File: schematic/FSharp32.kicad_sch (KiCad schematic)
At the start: 17 parts

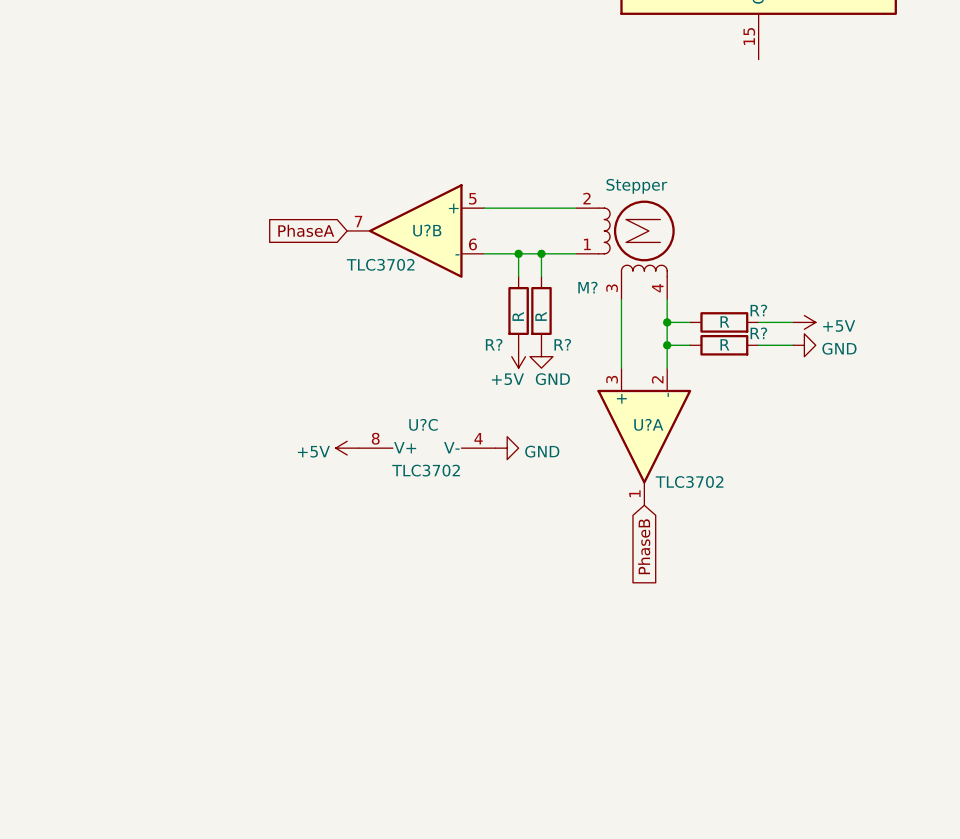
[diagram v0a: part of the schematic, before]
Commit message: continued schematic (finished rotary encoder)
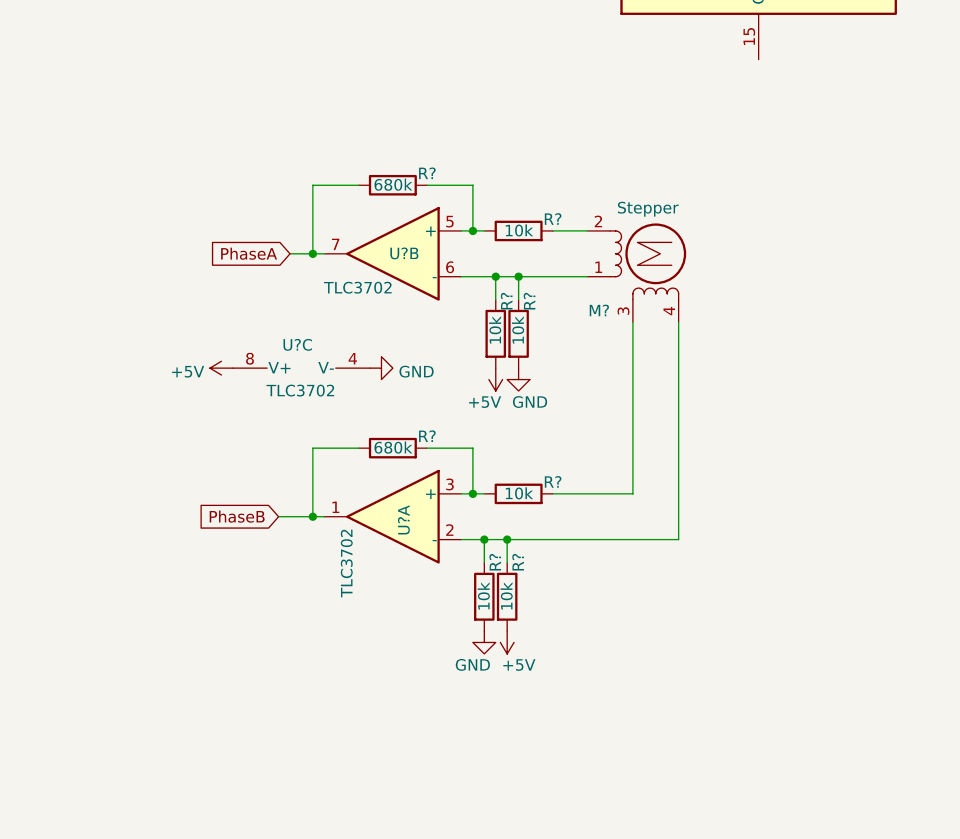
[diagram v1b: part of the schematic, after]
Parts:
- added R? (x2): 10k, symbol Device:R
- added R? (x2): 680k, symbol Device:R
- R? (x4): value R -> 10k
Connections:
- net PhaseA: now also R?.1
- net PhaseB: now also R?.1
- net at U?.5 (+): now also R?.1, R?.2; no longer M?.2 (-)
- net at U?.3 (+): now also R?.1, R?.2; no longer M?.3
- new net: M?.3, R?.2
- new net: M?.2 (-), R?.2
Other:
- moved on the sheet: M?, R?, U?A, U?B, U?C

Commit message: progress on schematic
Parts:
- removed R?: R, symbol Device:R
- removed U?: MP7524, symbol Flo:MP7524
- added C? (x5): 94p, symbol Device:C
- added C? (x2): 18p, symbol Device:C
- added C?: 100n, symbol Device:C
- added L? (x5): 56m, symbol Device:L
- added R? (x25): 4.7k, symbol Device:R
- added U? (x3): MCP6002-xSN, symbol Amplifier_Operational:MCP6002-xSN
- added Y?: 16M, symbol Device:Crystal
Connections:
- net +5V: now also C?.1
- net GND: now also C?.1, C?.1, C?.2, C?.2, C?.2, C?.2, C?.2, C?.2, R?.2
- net at U?.12 (XTAL2): now also C?.2, Y?.2
- net at U?.13 (XTAL1): now also C?.2, Y?.1
- net DAC7: now reaches U?.33 (PA7)
- net DAC7: now also R?.1
- net DAC6: now reaches U?.34 (PA6)
- net DAC6: now also R?.1
- net DAC5: now reaches U?.35 (PA5)
- net DAC5: now also R?.1
- net DAC4: now reaches U?.36 (PA4)
- net DAC4: now also R?.1
- net DAC3: now reaches U?.37 (PA3)
- net DAC3: now also R?.1
- net DAC2: now reaches U?.38 (PA2)
- net DAC2: now also R?.1
- net DAC1: now reaches U?.39 (PA1)
- net DAC1: now also R?.1
- net DAC0: now reaches U?.40 (PA0)
- net DAC0: now also R?.1
- net Vivrato renamed Vibrato
- new net: R?.1, R?.2 (x10)
- new net: C?.1, L?.2, U?.5 (+)
- new net: U?.6 (-), U?.7
- new net: C?.1, L?.1, L?.2 (x4)
- new net: R?.1, R?.2, R?.2 (x7)
- no-connect marks 3 -> 0
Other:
- moved on the sheet: M?, R?, SW?, U?, U?A, U?B, U?C

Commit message: progress schematic
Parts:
- removed SW?: SW_DIP_x04, symbol Switch:SW_DIP_x04
- added C?: C_Polarized, symbol Device:C_Polarized
- added C? (x2): C, symbol Device:C
- added DISTORTION: 100k, symbol Device:R_Potentiometer
- added R? (x2): R, symbol Device:R
- added R? (x2): 56k, symbol Device:R
- added U?: LM4861, symbol Flo:LM4861
- added VOLUME: 1k, symbol Device:R_Potentiometer
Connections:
- net +5V: now also U?.8 (V+), R?.1, U?.6 (Vcc)
- net GND: now also U?.4 (V-), C?.2, R?.2, U?.7 (GND)
- net at U?.6 (-), U?.7: now also C?.1
- net at R?.1, R?.2: now also C?.2
- net at L?.1: now also U?.1, R?.2
- net at U?.2 (-): now also DISTORTION.2
- net at U?.3 (+): now also R?.1, R?.2
- new net: C?.1, U?.2 (BP), U?.3 (+)
- new net: DISTORTION.1, R?.1
- new net: C?.1, DISTORTION.3
- new net: R?.1, U?.4 (-), VOLUME.1
- new net: C?.2, R?.2
- new net: U?.5 (Out1), VOLUME.2, VOLUME.3
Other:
- moved on the sheet: C?, L?, R?, U?, U?A, U?B, U?C

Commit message: schematic progress
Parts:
- removed R? (x22): 4.7k, symbol Device:R
- added J?: AudioJack2_Ground, symbol Connector:AudioJack2_Ground
- added J?: SerialPort, symbol Connector:DB9_Male_MountingHoles
- added LS?: Speaker, symbol Device:Speaker
- added R? (x7): 2k, symbol Device:R
- added R? (x6): 1k, symbol Device:R
- added SW?: ~, symbol Switch:SW_SPDT_MSM
- added SW? (x2): ~, symbol Switch:SW_DPDT_x2
- added SW? (x2): ~, symbol Switch:SW_DIP_x01
- R? (x2): value 4.7k -> 2k
- R?: value 4.7k -> 1k
- SW?: value MenuBtn -> MENU
- SW?: value BackBtn -> BACK
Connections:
- net +5V: now also U?.16 (VCC)
- net DAC0: now also R?.1
- net DAC1: now also R?.1
- net DAC2: now also R?.1
- net DAC3: now also R?.1
- net DAC4: now also R?.1
- net DAC5: now also R?.1
- net DAC6: now also R?.1
- net DAC7: now also R?.1
- net GND: now also R?.2, U?.15 (GND), J?.0 (PAD), J?.5, SW?.1, SW?.1, SW?.2
- net OctaveSetting0: now also SW?.2
- net OctaveSetting1: now also SW?.2
- net Rx: now also U?.9 (R2OUT)
- net Tremolo: now also SW?.1
- net Tx: now also U?.10 (T2IN)
- net Vibrato: now also SW?.3
- net at R?.1, R?.2: now also R?.2
- net at C?.2, R?.1: now also R?.2
- net at R?.2: now also R?.1, R?.2
- net at U?.5 (Out1), VOLUME.2, VOLUME.3: now also SW?.2 (B)
- net at U?.7 (T2OUT): now also J?.2
- net at U?.8 (R2IN): now also J?.3
- net at U?.8 (Out2): now also SW?.5 (B)
- new net: R?.1, R?.2, R?.2 (x5)
- new net: LS?.1, SW?.4 (A)
- new net: LS?.2, SW?.1 (A)
- new net: J?.S, J?.T, SW?.3 (C)
- new net: J?.G, SW?.6 (C)
- no-connect marks 0 -> 6
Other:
- moved on the sheet: U?

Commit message: schematic finalized (next footprints)
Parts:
- added C?: 10u, symbol Device:C
- added C? (x3): 10u, symbol Device:C_Polarized
- added C? (x2): 100n, symbol Device:C
- added C? (x2): 100u, symbol Device:C
- added J?: POWER, symbol Connector:Screw_Terminal_01x02
- added J?: PICkit2, symbol Connector:Conn_01x06_Male
- added R?: 2k, symbol Device:R
- C?: value C_Polarized -> 10u
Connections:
- net +5V: now also C?.1, C?.1, C?.1, C?.1, C?.1, J?.1 (Pin_1), J?.2 (Pin_2), R?.1
- net GND: now also C?.1, C?.2, C?.2, C?.2, C?.2, C?.2, C?.2, J?.2 (Pin_2), J?.3 (Pin_3)
- net MISO: now also J?.6 (Pin_6)
- net MOSI: now also J?.4 (Pin_4)
- net RESET: now also J?.1 (Pin_1), R?.2
- net at U?.2 (VS+): now also C?.1
- net at U?.4 (C2+): now also C?.1
- net at U?.5 (C2-): now also C?.2
- net at U?.6 (VS-): now also C?.2
- new net SCK: J?.5 (Pin_5)
- no-connect marks 6 -> 12
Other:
- title: (none) -> FSharp32
- moved on the sheet: J?

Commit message: begun pcb
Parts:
- removed M?: Matrix4x8, symbol Flo:Matrix4x8
- removed R?: 2k, symbol Device:R
- removed U?: LM4861, symbol Flo:LM4861
- added C20, C21: 100n, Capacitor_THT:C_Rect_L4.0mm_W2.5mm_P2.50mm, symbol Device:C
- added F1: Fuse, Fuse:Fuse_2010_5025Metric, symbol Device:Fuse
- added J5: MatrixCols, Connector_PinHeader_2.54mm:PinHeader_1x08_P2.54mm_Vertical, symbol Connector:Conn_01x08_Pin
- added J6: MatrixRows, Connector_PinHeader_2.54mm:PinHeader_1x04_P2.54mm_Vertical, symbol Connector:Conn_01x04_Pin
- added U6: LM4861, Package_SO:SOIC-8_3.9x4.9mm_P1.27mm, symbol Flo:LM4861
- C1, C19, C3, C4, C5: renamed from C?; footprint (none) -> Capacitor_THT:CP_Radial_Tantal_D5.0mm_P2.50mm
- C10, C18, C2, C6, C9: renamed from C?; footprint (none) -> Capacitor_THT:C_Rect_L4.0mm_W2.5mm_P2.50mm
- C11, C17: renamed from C?; footprint (none) -> Capacitor_SMD:C_0805_2012Metric
- C12, C13, C14, C15, C16: renamed from C?; footprint (none) -> Capacitor_THT:C_Rect_L7.0mm_W2.0mm_P5.00mm
- C7, C8: renamed from C?; footprint (none) -> Capacitor_THT:CP_Radial_D10.0mm_P5.00mm
- DISTORTION1: renamed from DISTORTION; footprint (none) -> Connector_PinHeader_2.54mm:PinHeader_1x03_P2.54mm_Vertical
- J1: renamed from J?; footprint (none) -> Connector_Dsub:DSUB-9_Male_Horizontal_P2.77x2.84mm_EdgePinOffset7.70mm_Housed_MountingHolesOffset9.12mm
- J2: renamed from J?; footprint (none) -> Connector_PinHeader_2.54mm:PinHeader_1x06_P2.54mm_Vertical
- J3: renamed from J?; footprint (none) -> Connector_Audio:Jack_3.5mm_Lumberg_1503_07_Horizontal
- J4: renamed from J?; footprint (none) -> TerminalBlock:TerminalBlock_bornier-2_P5.08mm
- L1: renamed from L?; footprint (none) -> Inductor_THT:L_Axial_L6.6mm_D2.7mm_P10.16mm_Horizontal_Vishay_IM-2
- L2, L3, L4, L5: renamed from L?; footprint (none) -> Inductor_THT:L_Axial_L5.3mm_D2.2mm_P7.62mm_Horizontal_Vishay_IM-1
- LS1: renamed from LS?; footprint (none) -> TerminalBlock:TerminalBlock_bornier-2_P5.08mm
- M1: renamed from M?; footprint (none) -> Connector_PinSocket_2.54mm:PinSocket_1x04_P2.54mm_Vertical
- R1, R2, R3, R4, R5, R6, R8, R9: renamed from R?; footprint (none) -> Resistor_THT:R_Axial_DIN0204_L3.6mm_D1.6mm_P7.62mm_Horizontal
- R10, R13, R15, R21: renamed from R?; footprint (none) -> Resistor_SMD:R_0805_2012Metric
- R11, R12, R14, R16, R17, R18, R19, R20, R22, R23, R24, R25, R26, R27, R28, R29: renamed from R?; footprint (none) -> Resistor_THT:R_Axial_DIN0207_L6.3mm_D2.5mm_P7.62mm_Horizontal
- SW1: renamed from SW?; footprint (none) -> Connector_PinSocket_2.54mm:PinSocket_1x03_P2.54mm_Vertical
- SW2, SW3: renamed from SW?; footprint (none) -> Connector_PinHeader_2.54mm:PinHeader_1x02_P2.54mm_Vertical
- SW4, SW5: renamed from SW?; footprint (none) -> Connector_PinSocket_2.54mm:PinSocket_1x02_P2.54mm_Vertical
- SW6: renamed from SW?; footprint (none) -> Connector_PinSocket_2.54mm:PinSocket_2x03_P2.54mm_Vertical
- U1: renamed from U?; footprint (none) -> Package_DIP:DIP-8_W7.62mm
- U2: renamed from U?; footprint (none) -> Package_DIP:DIP-16_W7.62mm
- U3: renamed from U?; footprint (none) -> Connector_PinHeader_2.54mm:PinHeader_1x03_P2.54mm_Vertical
- U5: renamed from U?; footprint (none) -> Connector_PinHeader_2.54mm:PinHeader_1x04_P2.54mm_Vertical
- VOLUME1: renamed from VOLUME; footprint (none) -> Connector_PinHeader_2.54mm:PinHeader_1x03_P2.54mm_Vertical
- Y1: renamed from Y?; footprint (none) -> Crystal:Resonator-2Pin_W10.0mm_H5.0mm
- gave numbers to parts that had none: 1
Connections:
- net SCK is gone; now on net CLK: J2.5 (Pin_5)
- net +5V: now also F1.1, U6.6 (Vcc); no longer J4.1 (Pin_1)
- net BackBtn: now also C21.1
- net CLK: now also J5.8 (Pin_8)
- net GND: now also C20.2, C21.2, U6.7 (GND)
- net MISO: now also J5.7 (Pin_7)
- net MOSI: now also J5.6 (Pin_6)
- net MenuBtn: now also C20.1
- net Row0: now also J6.1 (Pin_1)
- net Row1: now also J6.2 (Pin_2)
- net Row2: now also J6.3 (Pin_3)
- net Row3: now also J6.4 (Pin_4)
- net at C19.1: now also U6.2 (BP), U6.3 (+)
- net at U4.1 (PB0): now also J5.1 (Pin_1)
- net at U4.2 (PB1): now also J5.2 (Pin_2)
- net at U4.3 (PB2): now also J5.3 (Pin_3)
- net at U4.4 (PB3): now also J5.4 (Pin_4)
- net at U4.5 (PB4): now also J5.5 (Pin_5)
- net at R21.1, VOLUME1.1: now also U6.4 (-)
- net at SW6.2 (B), VOLUME1.2, VOLUME1.3: now also U6.5 (Out1)
- net at SW6.5 (B): now also U6.8 (Out2)
- new net: F1.2, J4.1 (Pin_1)
- no-connect marks 12 -> 13
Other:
- moved on the sheet: C2, J2, J4, M1, R1, R2, R3, R4, R5, R6, R8, R9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

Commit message: pcb progress
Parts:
- DISTORTION1: footprint Connector_PinHeader_2.54mm:PinHeader_1x03_P2.54mm_Vertical -> Connector_PinSocket_2.54mm:PinSocket_1x02_P2.54mm_Vertical
- J1: renamed from J2; footprint Connector_PinHeader_2.54mm:PinHeader_1x06_P2.54mm_Vertical -> Connector_PinSocket_2.54mm:PinSocket_1x06_P2.54mm_Horizontal
- J3: renamed from J5; footprint Connector_PinHeader_2.54mm:PinHeader_1x08_P2.54mm_Vertical -> Connector_PinSocket_2.54mm:PinSocket_1x08_P2.54mm_Vertical
- J4: renamed from J6; footprint Connector_PinHeader_2.54mm:PinHeader_1x04_P2.54mm_Vertical -> Connector_PinSocket_2.54mm:PinSocket_1x04_P2.54mm_Vertical
- L2, L3, L4, L5: footprint Inductor_THT:L_Axial_L5.3mm_D2.2mm_P7.62mm_Horizontal_Vishay_IM-1 -> Inductor_THT:L_Axial_L6.6mm_D2.7mm_P10.16mm_Horizontal_Vishay_IM-2
- SW2, SW3: footprint Connector_PinHeader_2.54mm:PinHeader_1x02_P2.54mm_Vertical -> Connector_PinSocket_2.54mm:PinSocket_1x02_P2.54mm_Vertical
- U3: footprint Connector_PinHeader_2.54mm:PinHeader_1x03_P2.54mm_Vertical -> Package_SO:SOIC-8_3.9x4.9mm_P1.27mm
- U5: footprint Connector_PinHeader_2.54mm:PinHeader_1x04_P2.54mm_Vertical -> Connector_PinSocket_2.54mm:PinSocket_1x04_P2.54mm_Vertical
- VOLUME1: footprint Connector_PinHeader_2.54mm:PinHeader_1x03_P2.54mm_Vertical -> Connector_PinSocket_2.54mm:PinSocket_1x03_P2.54mm_Vertical
- renumbered C2 to C1, C8 to C10, C9 to C11, C10 to C12, C11 to C13, C12 to C14, C13 to C15, C14 to C16, C15 to C17, C16 to C18, C17 to C19, C1 to C2, C18 to C20, C19 to C21, C20 to C4, C21 to C5, C4 to C6, C5 to C7, C6 to C8, C7 to C9, J1 to J2, J3 to J5, J4 to J6, R11 to R10, R12 to R11, R13 to R12, R14 to R13, R15 to R14, R16 to R15, R17 to R16, R18 to R17, R19 to R18, R20 to R19, R21 to R20, R22 to R21, R23 to R22, R24 to R23, R25 to R24, R26 to R25, R27 to R26, R28 to R27, R29 to R28, R8 to R7, R9 to R8, R10 to R9
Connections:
- net at U3.6 (-), U3.7: now also C19.2; no longer C19.1
- net at R20.1, U6.4 (-): now also VOLUME1.3; no longer VOLUME1.1
- net at R20.2: now also C19.1; no longer C19.2
- net at SW6.2 (B), U6.5 (Out1), VOLUME1.2: now also VOLUME1.1; no longer VOLUME1.3
- net at SW6.6 (C): now also J5.R; no longer J5.G
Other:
- moved on the sheet: C2, VOLUME1

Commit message: continued pcb
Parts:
- removed VOLUME1: 1k, Connector_PinSocket_2.54mm:PinSocket_1x03_P2.54mm_Vertical, symbol Device:R_Potentiometer
- added VOLUME1: 1k, Connector_PinSocket_2.54mm:PinSocket_1x02_P2.54mm_Vertical, symbol Device:R_Variable
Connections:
- net at R2.2: now also M1.1; no longer M1.2 (-)
- net at R20.1, U6.4 (-): now also VOLUME1.2
- net at SW6.2 (B), U6.5 (Out1): now also VOLUME1.1
- net at R3.1, R4.1, U1.6 (-): now also M1.2 (-); no longer M1.1
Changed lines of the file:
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@@
     (title "FSharp32")
   )
-  (junction (at 232.41 127) (diameter 0) (color 0 0 0 0)
-  )
   (junction (at 256.54 134.62) (diameter 0) (color 0 0 0 0)
   )
@@
   (junction (at 91.44 100.33) (diameter 0) (color 0 0 0 0)
   )
+  (junction (at 132.08 60.96) (diameter 0) (color 0 0 0 0)
+  )
   (junction (at 146.05 99.06) (diameter 0) (color 0 0 0 0)
   )
@@
   (junction (at 54.61 24.13) (diameter 0) (color 0 0 0 0)
   )
-  (junction (at 133.35 31.75) (diameter 0) (color 0 0 0 0)
-  )
   (junction (at 146.05 170.18) (diameter 0) (color 0 0 0 0)
   )
   (junction (at 31.75 73.66) (diameter 0) (color 0 0 0 0)
   )
+  (junction (at 133.35 31.75) (diameter 0) (color 0 0 0 0)
+  )
   (junction (at 88.9 97.79) (diameter 0) (color 0 0 0 0)
   )
@@
   (junction (at 110.49 29.21) (diameter 0) (color 0 0 0 0)
   )
-  (junction (at 132.08 60.96) (diameter 0) (color 0 0 0 0)
-  )
   (junction (at 146.05 139.7) (diameter 0) (color 0 0 0 0)
   )
@@
     (stroke (width 0) (type default))
   )
+  (wire (pts (xy 146.05 36.83) (xy 146.05 55.88))
+    (stroke (width 0) (type default))
+  )
   (wire (pts (xy 243.84 55.88) (xy 262.89 55.88))
     (stroke (width 0) (type default))
@@
     (stroke (width 0) (type default))
   )
+  (wire (pts (xy 133.35 31.75) (xy 137.16 31.75))
+    (stroke (width 0) (type default))
+  )
   (wire (pts (xy 226.06 130.81) (xy 232.41 130.81))
     (stroke (width 0) (type default))
@@
     (stroke (width 0) (type default))
   )
-  (wire (pts (xy 151.13 60.96) (xy 151.13 36.83))
-    (stroke (width 0) (type default))
-  )
   (wire (pts (xy 255.27 110.49) (xy 270.51 110.49))
     (stroke (width 0) (type default))
@@
     (stroke (width 0) (type default))
   )
-  (wire (pts (xy 146.05 55.88) (xy 137.16 55.88))
-    (stroke (width 0) (type default))
-  )
   (wire (pts (xy 91.44 100.33) (xy 95.25 100.33))
     (stroke (width 0) (type default))
@@
     (stroke (width 0) (type default))
   )
+  (wire (pts (xy 146.05 55.88) (xy 137.16 55.88))
+    (stroke (width 0) (type default))
+  )
   (wire (pts (xy 20.32 73.66) (xy 22.86 73.66))
     (stroke (width 0) (type default))
@@
     (stroke (width 0) (type default))
   )
+  (wire (pts (xy 137.16 31.75) (xy 140.97 26.67))
+    (stroke (width 0) (type default))
+  )
   (wire (pts (xy 212.09 140.97) (xy 215.9 140.97))
     (stroke (width 0) (type default))
@@
     (stroke (width 0) (type default))
   )
-  (wire (pts (xy 133.35 31.75) (xy 140.97 31.75))
-    (stroke (width 0) (type default))
-  )
   (wire (pts (xy 69.85 97.79) (xy 88.9 97.79))
     (stroke (width 0) (type default))
@@
     (stroke (width 0) (type default))
   )
-  (wire (pts (xy 232.41 127) (xy 232.41 130.81))
+  (wire (pts (xy 232.41 123.19) (xy 232.41 130.81))
     (stroke (width 0) (type default))
   )
@@
     (stroke (width 0) (type default))
   )
-  (wire (pts (xy 146.05 36.83) (xy 146.05 55.88))
-    (stroke (width 0) (type default))
-  )
   (wire (pts (xy 207.01 128.27) (xy 207.01 129.54))
     (stroke (width 0) (type default))
@@
     (stroke (width 0) (type default))
   )
-  (wire (pts (xy 232.41 127) (xy 232.41 123.19))
-    (stroke (width 0) (type default))
-  )
   (wire (pts (xy 207.01 144.78) (xy 209.55 144.78))
     (stroke (width 0) (type default))
@@
     (stroke (width 0) (type default))
   )
-  (wire (pts (xy 236.22 127) (xy 232.41 127))
+  (wire (pts (xy 137.16 26.67) (xy 140.97 31.75))
     (stroke (width 0) (type default))
   )
@@
     (stroke (width 0) (type default))
   )
+  (wire (pts (xy 151.13 60.96) (xy 151.13 36.83))
+    (stroke (width 0) (type default))
+  )
   (wire (pts (xy 236.22 102.87) (xy 236.22 101.6))
     (stroke (width 0) (type default))
@@
     (stroke (width 0) (type default))
   )
-  (wire (pts (xy 137.16 26.67) (xy 140.97 26.67))
-    (stroke (width 0) (type default))
-  )
   (wire (pts (xy 146.05 160.02) (xy 146.05 161.29))
     (stroke (width 0) (type default))
@@
     )
   )
-  (symbol (lib_id "Device:R_Potentiometer") (at 236.22 123.19 90) (mirror x) (unit 1)
-    (in_bom yes) (on_board yes) (dnp no)
-    (property "Reference" "VOLUME1" (at 236.22 120.1436 90)
-      (effects (font (size 1.27 1.27)))
-    )
-    (property "Value" "1k" (at 236.22 123.19 90)
-      (effects (font (size 1.27 1.27)))
-    )
-    (property "Footprint" "Connector_PinSocket_2.54mm:PinSocket_1x03_P2.54mm_Vertical" (at 236.22 123.19 0)
-      (effects (font (size 1.27 1.27)) hide)
-    )
-    (property "Datasheet" "~" (at 236.22 123.19 0)
-      (effects (font (size 1.27 1.27)) hide)
-    )
-    (pin "1")
-    (pin "2")
-    (pin "3")
-    (instances
-      (project "FSharp32"
-        (path "/e39530c9-181c-4f36-a0a9-369d5d87e3f5"
-          (reference "VOLUME1") (unit 1)
-        )
-      )
-    )
-  )
   (symbol (lib_id "Device:R") (at 130.81 38.1 0) (unit 1)
     (in_bom yes) (on_board yes) (dnp no)
@@
         )
       )
+    )
+  )
+  (symbol (lib_id "Device:R_Variable") (at 236.22 123.19 90) (unit 1)
+    (in_bom yes) (on_board yes) (dnp no)
+    (property "Reference" "VOLUME1" (at 236.22 119.38 90)
+      (effects (font (size 1.27 1.27)))
+    )
+    (property "Value" "1k" (at 236.22 123.19 90)
+      (effects (font (size 1.27 1.27)))
+    )
+    (property "Footprint" "Connector_PinSocket_2.54mm:PinSocket_1x02_P2.54mm_Vertical" (at 236.22 124.968 90)
+      (effects (font (size 1.27 1.27)) hide)
+    )
+    (property "Datasheet" "~" (at 236.22 123.19 0)
+      (effects (font (size 1.27 1.27)) hide)
+    )
+    (pin "1")
+    (pin "2")
+    (instances
+      (project "FSharp32"
+        (path "/e39530c9-181c-4f36-a0a9-369d5d87e3f5"
+          (reference "VOLUME1") (unit 1)
+        )
+      )
